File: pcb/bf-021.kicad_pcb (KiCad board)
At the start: 2 copper layers, 50 x 50 mm, 12 parts, among them J1 M-BUS, U1 SCD40-D-R2

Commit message: improved design
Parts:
- R1, R2: value R -> 10k; footprint Resistor_THT:R_Axial_DIN0207_L6.3mm_D2.5mm_P7.62mm_Horizontal -> Resistor_SMD:R_0603_1608Metric_Pad0.98x0.95mm_HandSolder
- moved R2 11.9 mm to (115.0, 75.0), turned to -90 degrees
- moved R1 11.5 mm to (115.0, 71.0), turned to -90 degrees
- moved CO2-Sensor 9.55 mm to (125.1, 74.9), turned to 90 degrees
- renumbered U1 to CO2-Sensor
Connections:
- CO2-Sensor pad 10: /GPIO2 -> SDA
- CO2-Sensor pad 9: /GPIO5 -> SCL
- J1 pad 19: /GPIO5 -> SCL
- J1 pad 20: /GPIO2 -> SDA
- R1 pad 1: /GPIO5 -> +3V3
- R1 pad 2: GND -> SDA
- R2 pad 1: /GPIO2 -> SCL
- R2 pad 2: GND -> +3V3
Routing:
- net GND: track 123.9 -> 30.1 mm, vias 0 -> 1
- net /GPIO2: track 75.7 -> 0.00 mm, vias 2 -> 0
- net SDA: track 0.00 -> 60.3 mm
- net /GPIO5: track 45.3 -> 0.00 mm
- net SCL: track 0.00 -> 16.1 mm
- net +3V3: track 37.4 -> 48.4 mm
- added copper zone on F.Cu, net GND

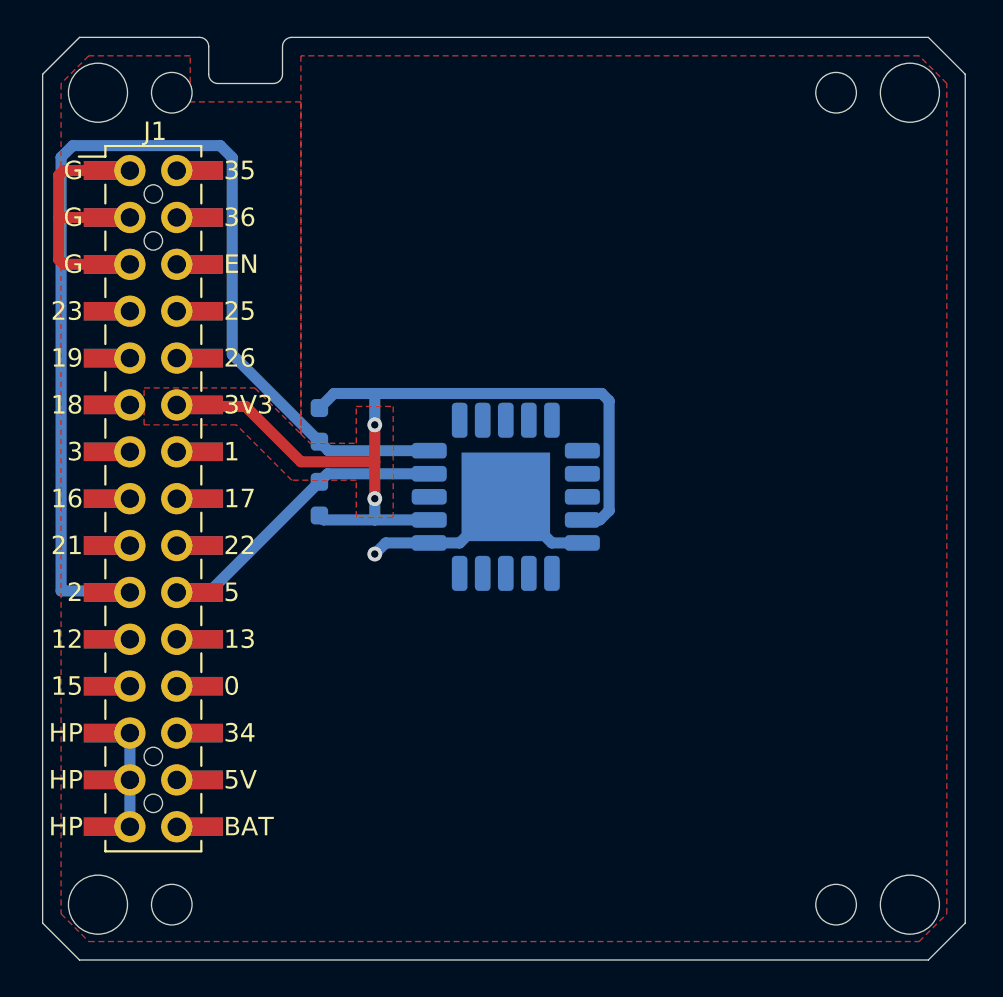
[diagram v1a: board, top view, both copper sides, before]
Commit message: fixed connector being on wrong side
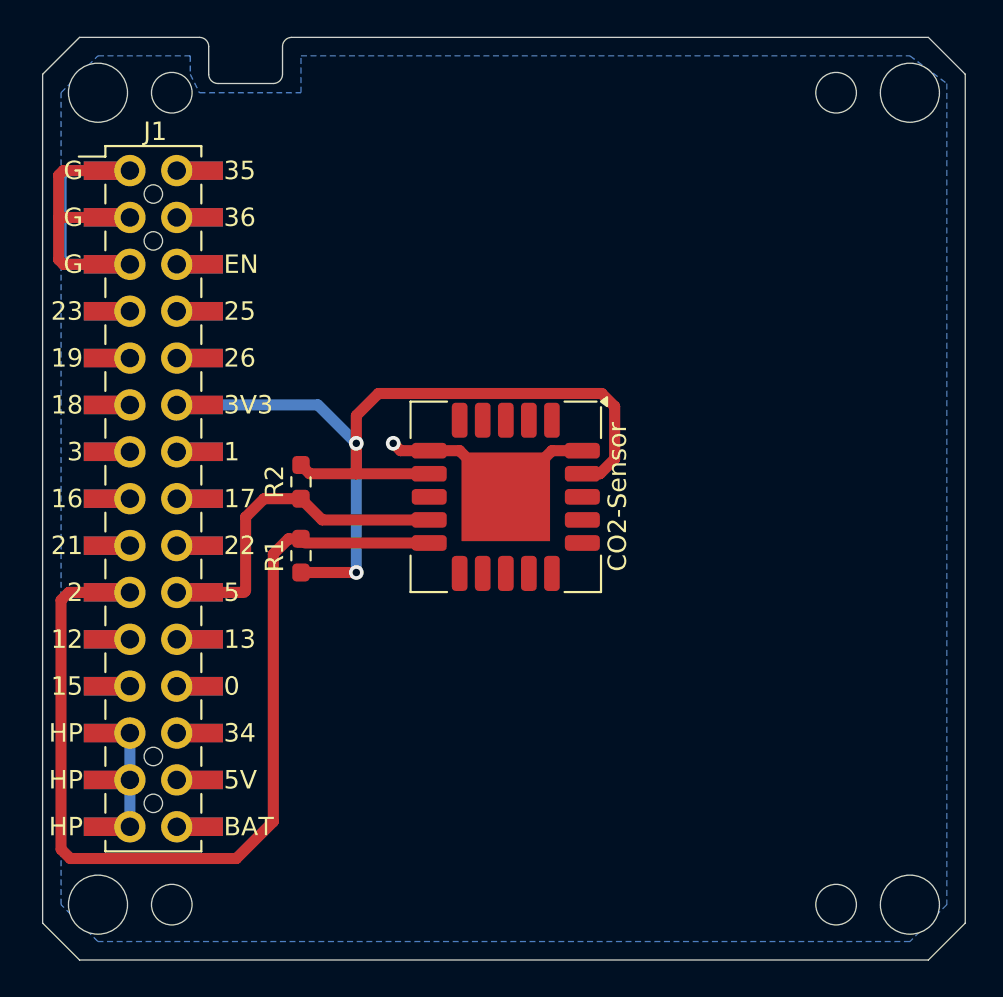
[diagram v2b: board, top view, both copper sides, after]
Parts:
- CO2-Sensor, R1, R2: moved to F.Cu
- moved R1 7.16 mm to (114.0, 78.1), turned to 90 degrees
- moved R2 1.35 mm to (114.0, 74.1), turned to 90 degrees
- turned CO2-Sensor to -90 degrees
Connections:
- CO2-Sensor pad 9: SCL -> SDA
- J1 pad 19: SCL -> SDA
- R2 pad 1: SCL -> SDA
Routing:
- net SCL: track 16.1 -> 0.00 mm
- net GND: track 30.1 -> 44.9 mm
- net SDA: track 60.3 -> 71.9 mm
- net +3V3: track 48.4 -> 50.6 mm
- added copper zone on B.Cu, net GND
- removed copper zone on F.Cu, net GND
